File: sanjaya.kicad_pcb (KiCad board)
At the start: 2 copper layers, 82 parts, among them J1 PWR_SUPPLY, J10 Bat_Bak_Byp_Gnd, J11 Board_PwrIn, J12 ON_Switch, J13 Raspberry_Pi_2_3, J14 Fan, J15 RS232, J16 RS485, J17 I2C, J18 Bat_Bak_Byp_Vcc, J2 Digital_Input_Signals, J3 Digital_Input_Gnd, J4 Screw_Terminal_01x03, J5 Screw_Terminal_01x03, J6 Analog_RSense, J7 Analog_420, J8 Supply_Safety_Bypass, J9 To_PwrBank, K1 Songle-SRD, K2 Songle-SRD, Q1 Q_PMOS_GSD, Q2 FDC021N30, SW2 SW_DIP_x04, U1 74HC14, U2 MCP9700T-ETT, U3 TPS2400BVR, U4 ULN2803A, U5 MCP3428, U6 TLP291-4, U7 MAX232, U8 SN65HVD75DR

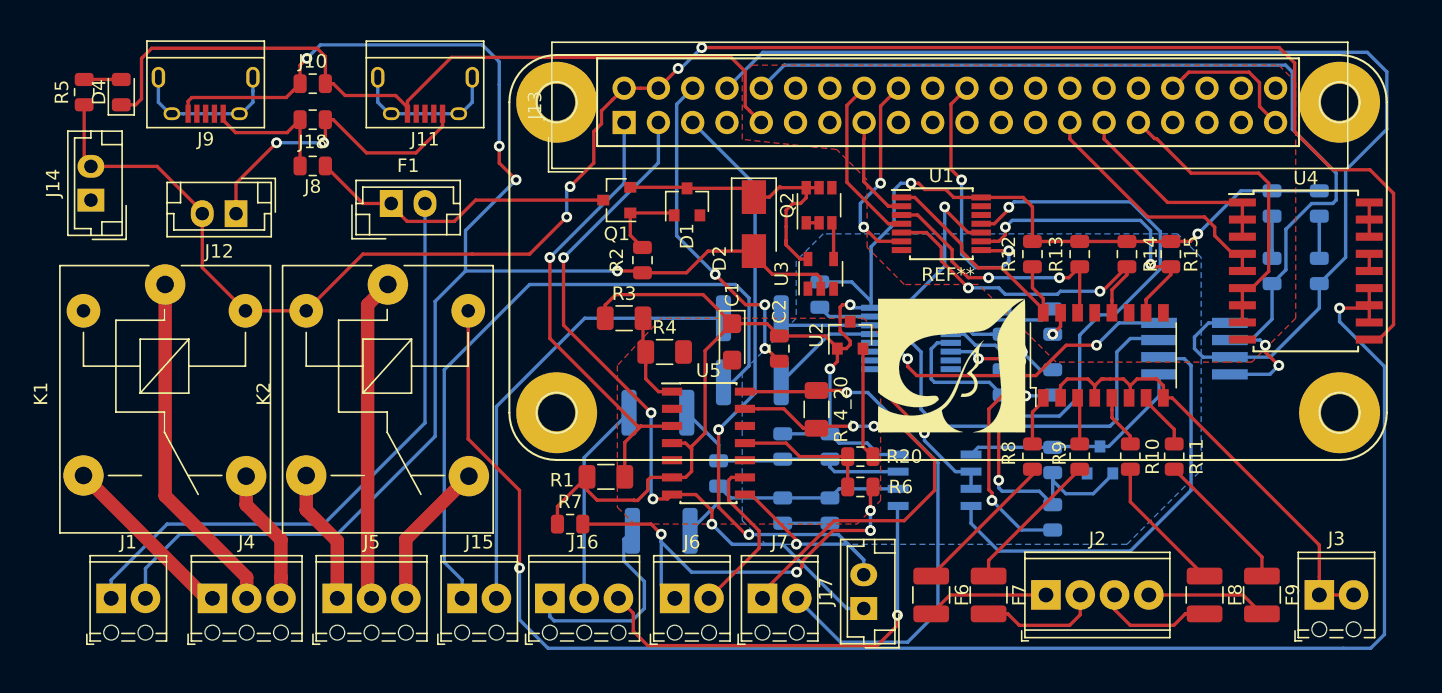
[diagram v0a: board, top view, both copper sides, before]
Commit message: All routing done. DRC is passing. NPTH and edge cut are the only things remaining.
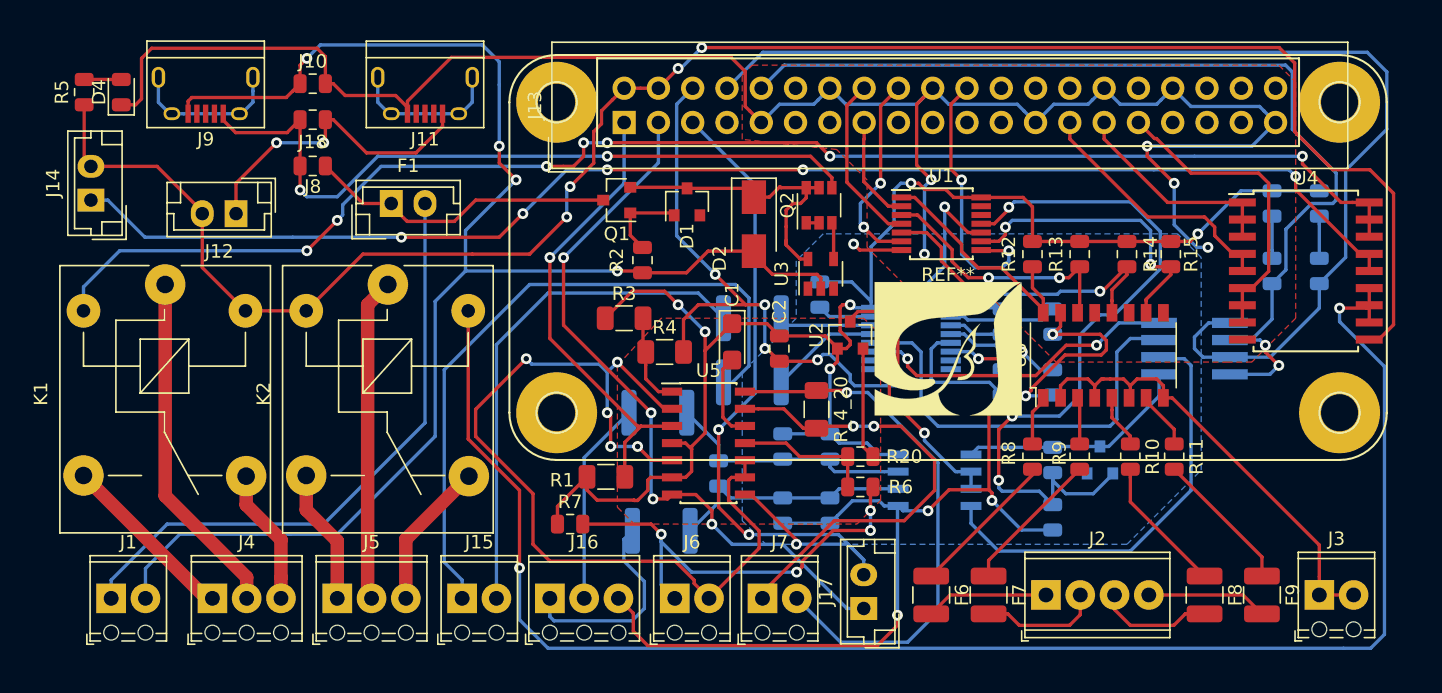
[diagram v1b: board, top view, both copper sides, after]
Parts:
- moved G*** 1.27 mm to (140.8, 106.2)
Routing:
- net Net-(K1-Pad2): track 2.54 -> 107.2 mm, vias 0 -> 7
- net Net-(J14-Pad1): track 1.27 -> 102.3 mm, vias 0 -> 5
- net /DGND: track 130.1 -> 226.6 mm, vias 4 -> 11
- net /AGND: track 37.3 -> 127.9 mm, vias 3 -> 10
- net Net-(J18-Pad2): track 10.4 -> 54.4 mm, vias 0 -> 2
- net /serial/RS232_TX: track 33.7 -> 38.0 mm
- net /3V3: track 121.5 -> 120.8 mm, vias 4 -> 6

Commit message: Changes: 1. NPTH, Edge cuts added 2. Labels for connectors added 3. DRC is passing
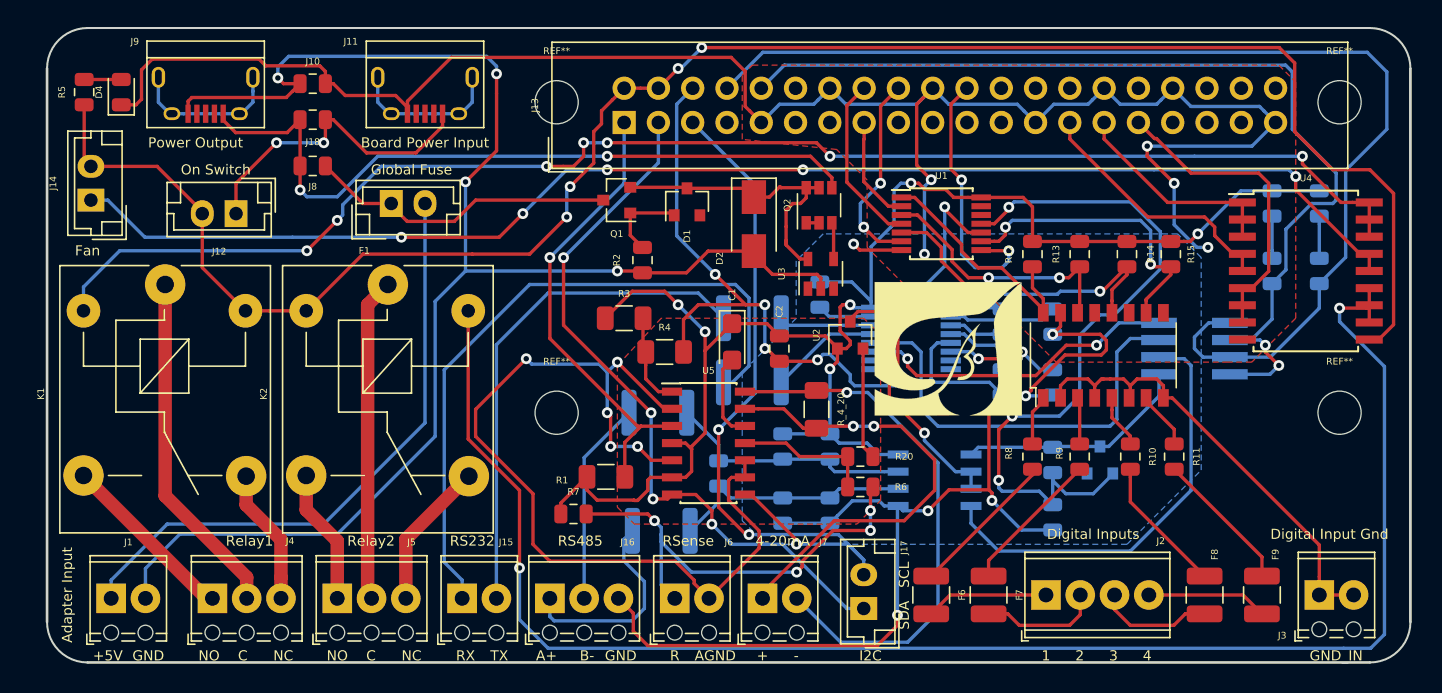
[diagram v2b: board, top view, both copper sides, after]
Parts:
- removed the REF** at (140.8, 99.5)
- added REF**: MountingHole_3.2mm_M3_DIN965, MountingHole:MountingHole_3.2mm_M3_DIN965, F.Cu at (111.8, 88.0)
- added REF**: MountingHole_3.2mm_M3_DIN965, MountingHole:MountingHole_3.2mm_M3_DIN965, F.Cu at (169.8, 88.0)
- added REF**: MountingHole_3.2mm_M3_DIN965, MountingHole:MountingHole_3.2mm_M3_DIN965, F.Cu at (169.8, 111.0)
- added REF**: MountingHole_3.2mm_M3_DIN965, MountingHole:MountingHole_3.2mm_M3_DIN965, F.Cu at (111.8, 111.0)
- moved R7 0.79 mm to (113.0, 118.5)
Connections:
- J11 pad 2: (no net) -> Net-(J11-Pad2)
- J11 pad 3: (no net) -> Net-(J11-Pad3)
- J11 pad 4: (no net) -> Net-(J11-Pad4)
- J13 pad 11: (no net) -> Net-(J13-Pad11)
- J13 pad 12: (no net) -> Net-(J13-Pad12)
- J13 pad 13: (no net) -> Net-(J13-Pad13)
- J13 pad 17: (no net) -> Net-(J13-Pad17)
- J13 pad 19: (no net) -> Net-(J13-Pad19)
- J13 pad 21: (no net) -> Net-(J13-Pad21)
- J13 pad 23: (no net) -> Net-(J13-Pad23)
- J13 pad 24: (no net) -> Net-(J13-Pad24)
- J13 pad 26: (no net) -> Net-(J13-Pad26)
- J13 pad 28: (no net) -> Net-(J13-Pad28)
- J13 pad 32: (no net) -> Net-(J13-Pad32)
- J13 pad 33: (no net) -> Net-(J13-Pad33)
- J13 pad 35: (no net) -> Net-(J13-Pad35)
- J13 pad 36: (no net) -> Net-(J13-Pad36)
- J13 pad 37: (no net) -> Net-(J13-Pad37)
- J13 pad 38: (no net) -> Net-(J13-Pad38)
- J13 pad 40: (no net) -> Net-(J13-Pad40)
- J13 pad 7: (no net) -> Net-(J13-Pad7)
- J9 pad 2: (no net) -> Net-(J9-Pad2)
- J9 pad 3: (no net) -> Net-(J9-Pad3)
- J9 pad 4: (no net) -> Net-(J9-Pad4)
- U3 pad 1: (no net) -> Net-(U3-Pad1)
- U3 pad 3: (no net) -> Net-(U3-Pad3)
- U7 pad 10: (no net) -> Net-(U7-Pad10)
- U7 pad 7: (no net) -> Net-(U7-Pad7)
- U7 pad 8: (no net) -> Net-(U7-Pad8)
- U7 pad 9: (no net) -> Net-(U7-Pad9)
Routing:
- net /DGND: track 226.6 -> 224.8 mm
- net /3V3: track 120.8 -> 119.9 mm
- net /powerSupply/Gnd_In: track 114.4 -> 115.1 mm
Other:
- board outline added: 101 x 47 mm
- board text added: "+"
- board text added: "+5V"
- board text added: "-"
- board text added: "1"
- board text added: "2"
- board text added: "3"
- board text added: "4"
- board text added: "4-20mA"
- board text added: "A+"
- board text added: "AGND"
- board text added: "Adapter Input"
- board text added: "B-"
- board text added: "Board Power Input"
- board text added: "C"
- board text added: "Digital Input Gnd"
- board text added: "Digital Inputs"
- board text added: "Fan"
- board text added: "GND"
- board text added: "GND_IN"
- board text added: "Global Fuse"
- board text added: "I2C"
- board text added: "NC"
- board text added: "NO"
- board text added: "On Switch"
- board text added: "Power Output"
- board text added: "R"
- board text added: "RS232"
- board text added: "RS485"
- board text added: "RSense"
- board text added: "RX"
- board text added: "Relay1"
- board text added: "Relay2"
- board text added: "SCL"
- board text added: "SDA"
- board text added: "TX"

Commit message: Changes: 1. Finalized layout after adding logo, symbols, labels, polarity 2. Changed version to 0.9 on all sch files.
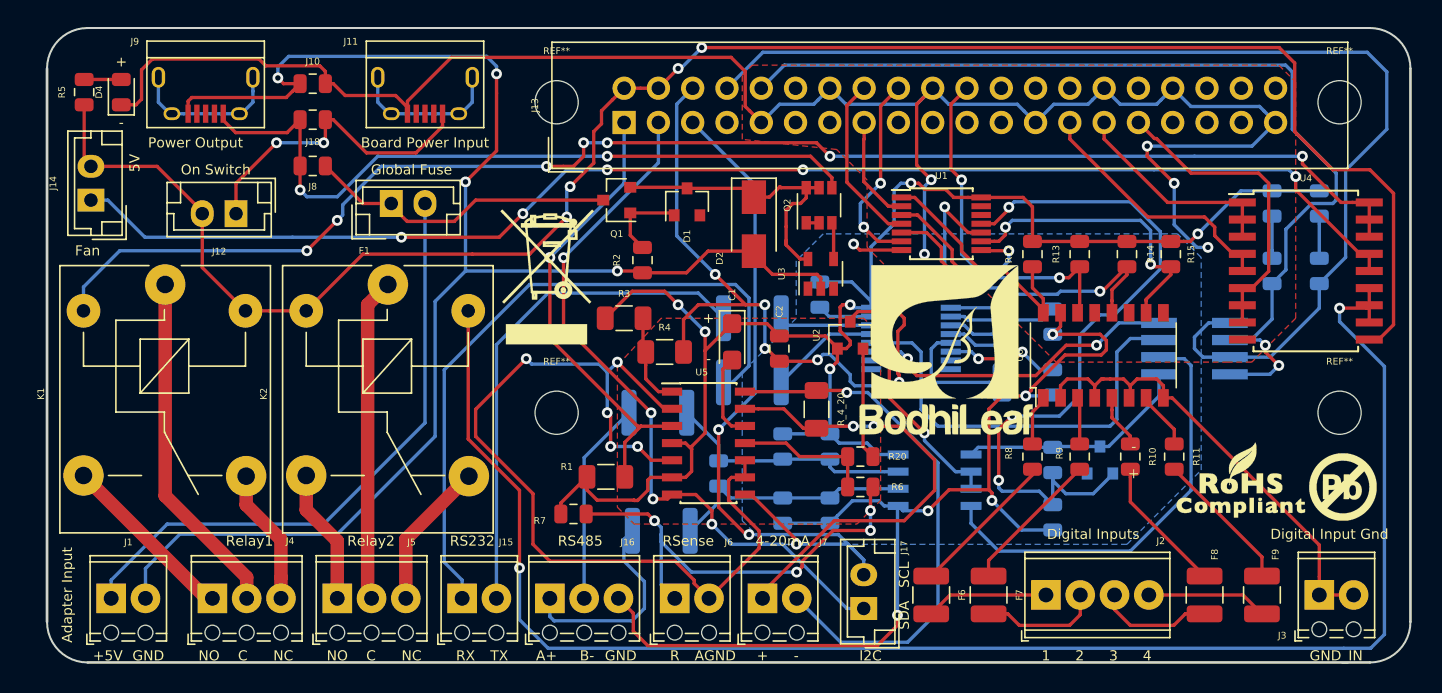
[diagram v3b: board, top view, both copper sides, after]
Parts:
- removed the G*** at (99.2, 109.5)
- added G***: LOGO, Custom Silkscreens:Logo_silk_WEEE_8x10mm, B.Cu at (99.5, 110.0)
- added G***: LOGO, Custom Silkscreens:Logo_silk_Lead-Free_5x5mm, B.Cu at (114.0, 102.5)
- added G***: LOGO, Custom Silkscreens:Logo_silk_ROHS_10x5.6mm, B.Cu at (114.0, 96.0)
- added G***: LOGO, Custom Silkscreens:bodhileafText, F.Cu at (140.5, 111.5)
- added G***: LOGO, Custom Silkscreens:bodhileafLogoAndText, B.Cu at (137.5, 96.0)
- added G***: LOGO, Custom Silkscreens:Logo_silk_Lead-Free_5x5mm, F.Cu at (170.0, 116.5)
- added G***: LOGO, Custom Silkscreens:Logo_silk_ROHS_10x5.6mm, F.Cu at (162.5, 116.0)
- added G***: LOGO, Custom Silkscreens:Logo_silk_WEEE_8x10mm, F.Cu at (111.0, 101.0)
- moved G*** 1.27 mm to (140.5, 105.0)
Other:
- board text added: "5V"

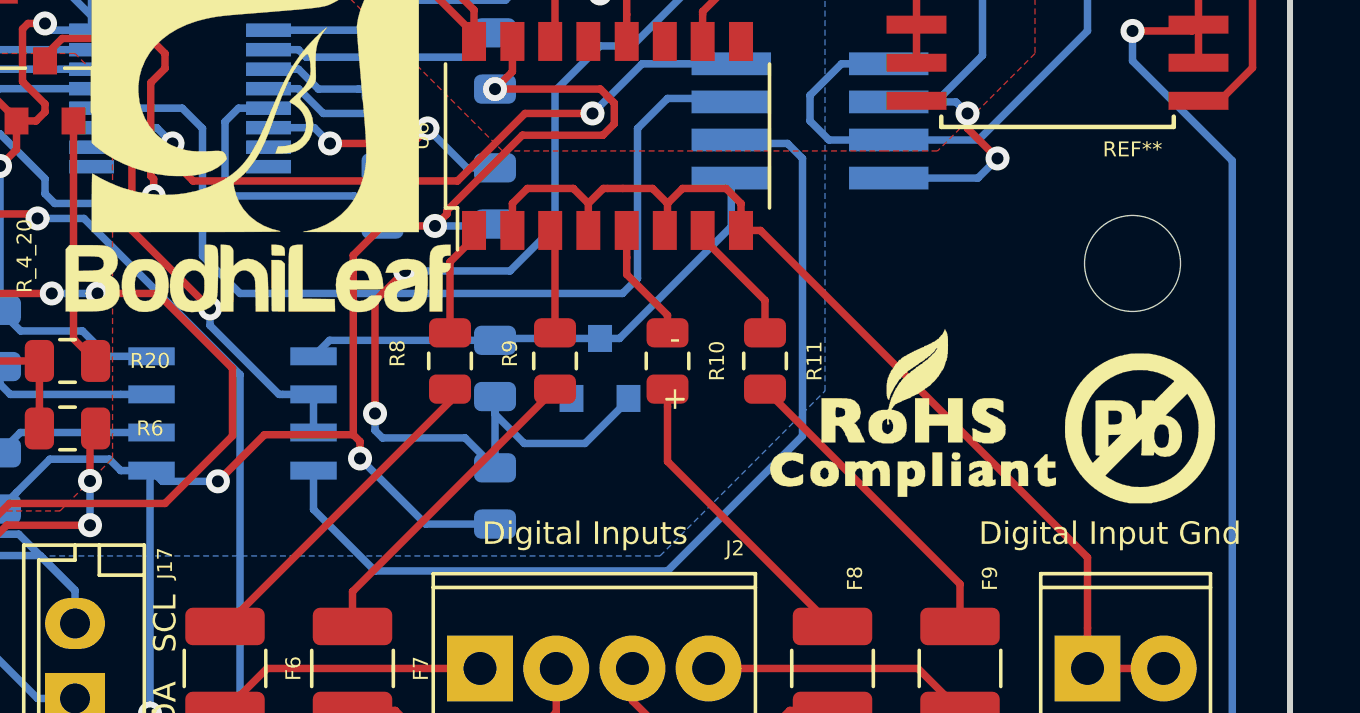
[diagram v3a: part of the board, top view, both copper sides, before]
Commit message: Changes: 1. Added CE logo to the front and back of the board 2. Plotted gerber files.
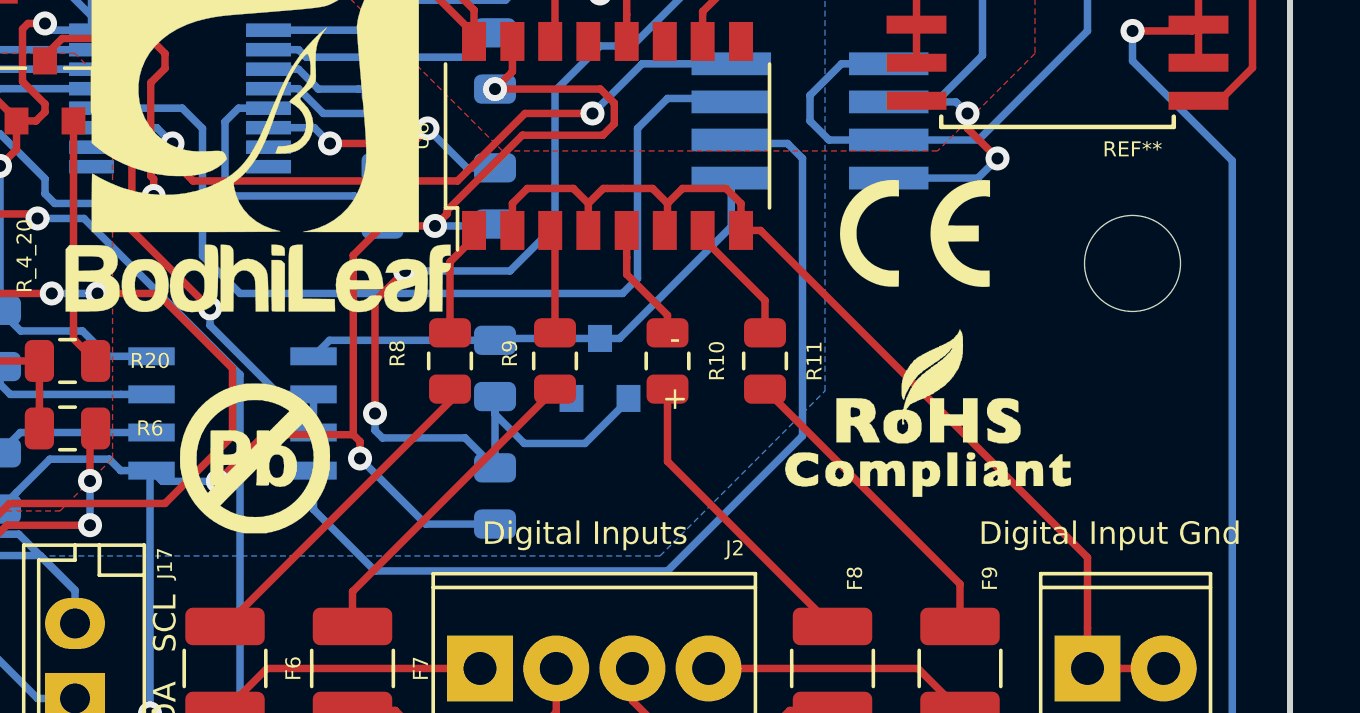
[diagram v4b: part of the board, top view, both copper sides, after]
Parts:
- added G***: LOGO, Custom Silkscreens:Logo_silk_CE_5x3.6mm, F.Cu at (162.5, 110.0)
- added G***: LOGO, Custom Silkscreens:Logo_silk_CE_5x3.6mm, B.Cu at (116.5, 98.0)
- moved G*** 31.8 mm to (83.0, 109.5)
- moved G*** 29.5 mm to (140.5, 117.5)
- moved G*** 8.73 mm to (116.0, 104.5)
- moved G*** 0.50 mm to (163.0, 116.0)
